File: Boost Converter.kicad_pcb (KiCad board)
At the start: 2 copper layers, 84.8 x 99.5 mm, 37 parts, among them IC2 UCC5304DWVR, J3 Conn_01x01_Pin, J4 Conn_01x01_Pin, J5 Conn_01x01_Pin, J6 Conn_01x01_Pin, J7 Conn_01x01_Pin, J8 Conn_01x01_Pin, Q1 STB11NK50ZT4, U1 Nucleo_L432KC

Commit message: Rerouted traces to avoid inductor. Added stitching vias, and silkscreen labels
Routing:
- net /Gate: track 49.4 -> 66.3 mm
- net /Switching_Node: track 49.1 -> 53.2 mm
- net /PWM: track 22.7 -> 24.7 mm
- net /Battery+_In: track 37.8 -> 39.8 mm
- net /Array+_In: track 66.2 -> 68.2 mm
- net GND_I: vias 0 -> 64
- added copper zone on B.Cu, net GND_I
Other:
- board text added: "+12v"
- board text added: "Array+"
- board text added: "Array-"
- board text added: "Battery+"
- board text added: "Battery-"
- board text added: "HV_GND"
- board text added: "MPPT Boost Converter Breakout Board Designed by Isaac Neideffer 09/16/2025"
- board text added: "Use 8 Amp Fuses"

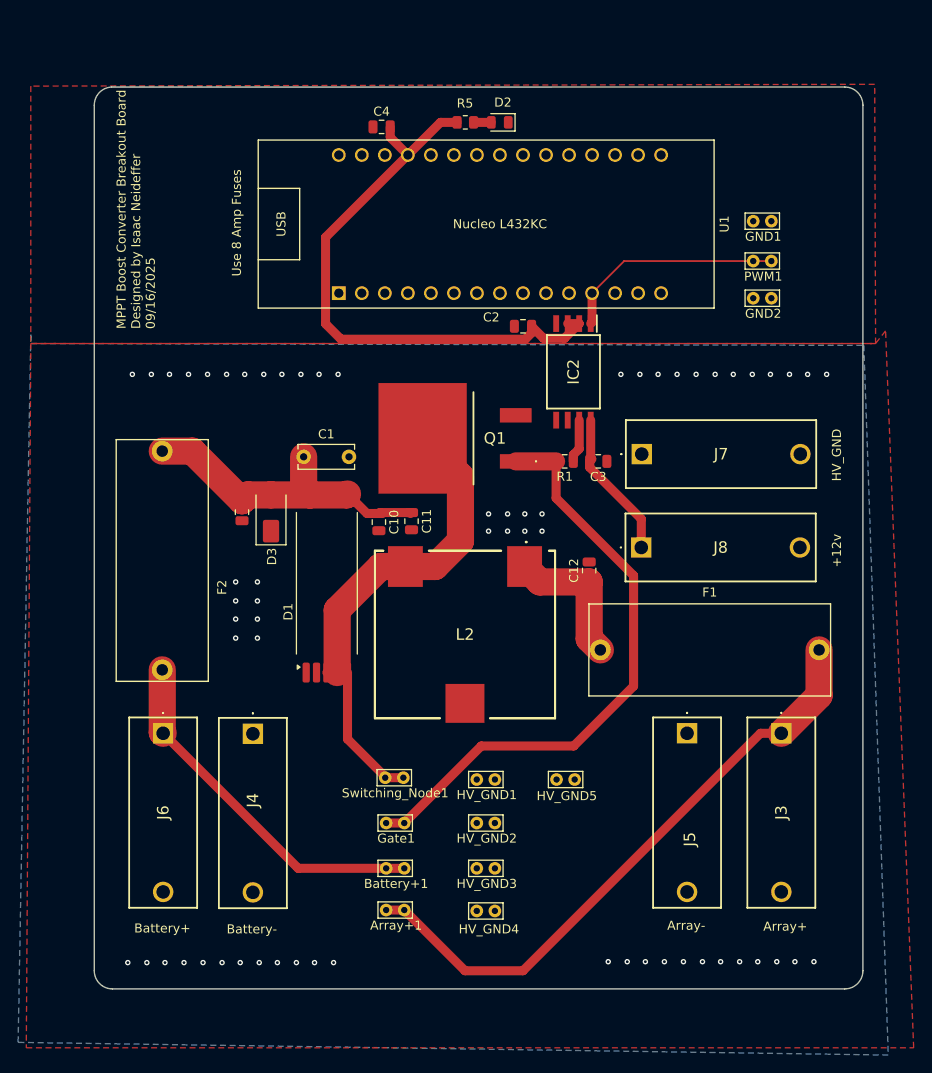
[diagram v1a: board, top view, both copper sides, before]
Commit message: New TVS diode, changed most traces to planes, added heatsink and thermal vias on mosfet. Made small adjustments to improve critical loop. Reworked some areas to shrink the board a little.
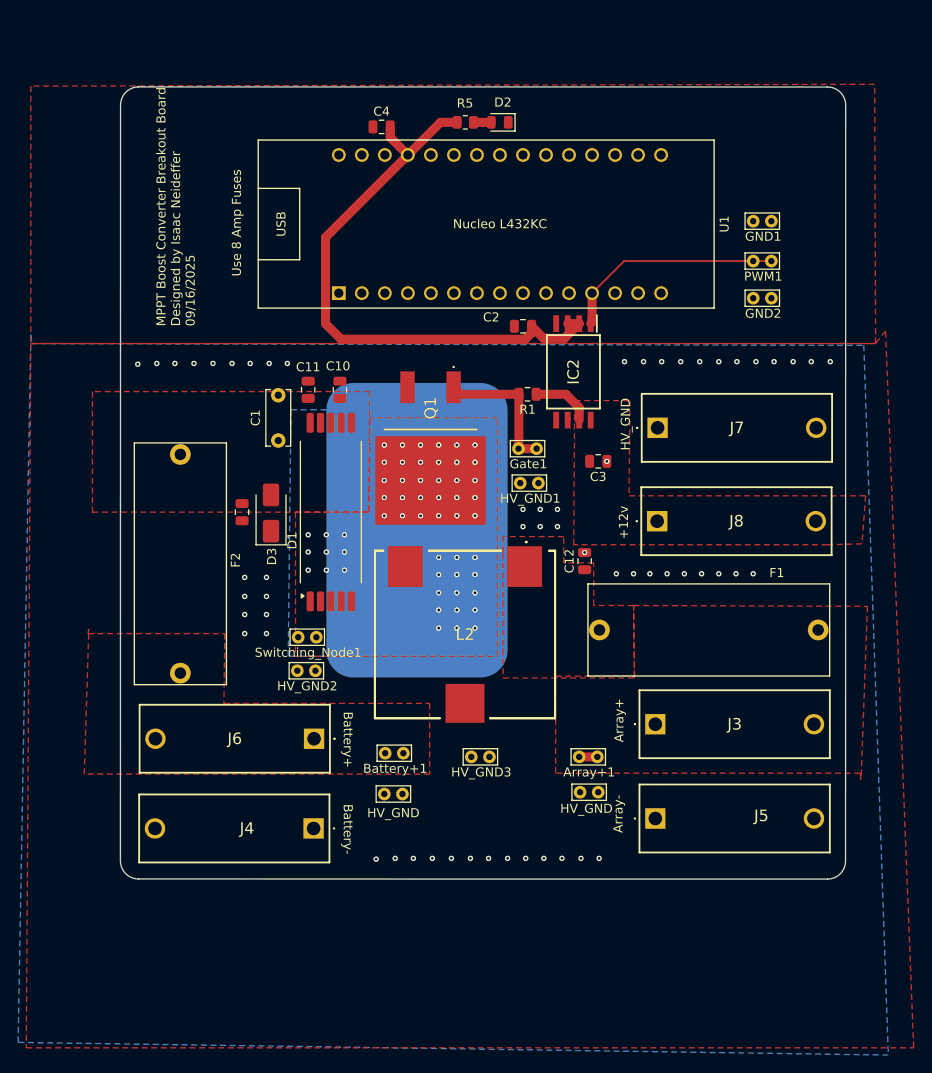
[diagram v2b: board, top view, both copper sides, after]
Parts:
- added HS1: Heatsink_Pad, My_Heatsink:HSE01-193175P, B.Cu at (109.4, 91.6)
- D3: value P4SMA200 -> P4SMA180CA
- F1, F2: value 10 Amp Fuse -> 7 Amp Fuse
- moved Gate1 43.8 mm to (121.6, 75.4)
- moved HV_GND1 33.1 mm to (121.8, 79.2)
- moved Array+1 27.2 mm to (128.3, 109.4)
- moved HV_GND2 26.0 mm to (97.2, 99.9)
- moved C11 18.4 mm to (98.4, 68.9), turned to 90 degrees
- moved Switching_Node1 18.2 mm to (97.3, 96.2)
- moved J6 16.7 mm to (99.0, 107.4), turned to 180 degrees
- moved Battery-1 16.4 mm to (106.8, 113.5)
- moved C10 15.2 mm to (101.9, 68.9), turned to 90 degrees
- moved J3 13.9 mm to (136.7, 105.8), turned to 0 degrees
- moved Battery+1 12.7 mm to (106.9, 109.0)
- moved J4 12.4 mm to (99.0, 117.3), turned to 180 degrees
- moved HV_GND3 12.3 mm to (116.4, 109.4)
- moved J5 10.0 mm to (136.7, 116.2), turned to 0 degrees
- moved R1 8.46 mm to (122.6, 69.4)
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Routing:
- net /Array+_In: track 68.2 -> 2.00 mm
- net /Switching_Node: track 53.2 -> 0.10 mm, vias 0 -> 54
- net /Gate: track 66.3 -> 15.6 mm
- net /Battery+_In: track 39.8 -> 0.00 mm
- net /Battery+: track 35.6 -> 0.00 mm
- net +12V: track 16.8 -> 0.00 mm
- net /Array+: track 15.8 -> 0.00 mm
- net Net-(IC2-OUT): track 4.82 -> 6.74 mm
- net GND_I: vias 64 -> 59
- added copper zone on F.Cu, net +12V
- added copper zone on F.Cu, net /Array+
- added copper zone on F.Cu, net /Array+_In
- added copper zone on F.Cu, net /Battery+
- added copper zone on F.Cu, net /Battery+_In
- added copper zone on B.Cu, net /Switching_Node
- added copper zone on F.Cu, net /Switching_Node
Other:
- board size 84.8 x 99.5 mm -> 80 x 87.4 mm
- board text removed: "HV_GND4"
- board text removed: "HV_GND5"
